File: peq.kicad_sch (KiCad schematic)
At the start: 0 parts

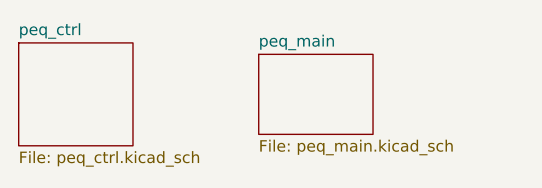
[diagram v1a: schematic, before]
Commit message: add protection components and fix layout
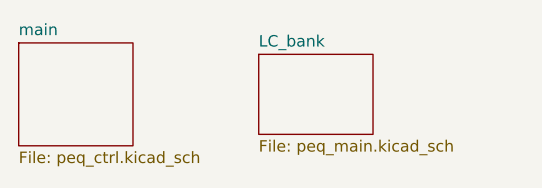
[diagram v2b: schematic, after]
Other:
- sheet peq_ctrl renamed main
- sheet peq_main renamed LC_bank
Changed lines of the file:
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@@
     (stroke (width 0.1524) (type solid) (color 0 0 0 0))
     (fill (color 0 0 0 0.0000))
-    (property "Sheet name" "peq_main" (id 0) (at 52.07 178.3584 0)
+    (property "Sheet name" "LC_bank" (id 0) (at 52.07 178.3584 0)
       (effects (font (size 1.27 1.27)) (justify left bottom))
     )
@@
     (stroke (width 0.1524) (type solid) (color 0 0 0 0))
     (fill (color 0 0 0 0.0000))
-    (property "Sheet name" "peq_ctrl" (id 0) (at 25.4 177.0884 0)
+    (property "Sheet name" "main" (id 0) (at 25.4 177.0884 0)
       (effects (font (size 1.27 1.27)) (justify left bottom))
     )
@@
       (reference "#FLG02") (unit 1) (value "PWR_FLAG") (footprint "")
     )
-    (path "/38f7f3f1-89e1-4fd2-a7f5-06bedaf10569/d5f17e22-8b80-4887-9e54-e1e00c7d3ac3"
+    (path "/bb76919e-6bfc-4ffb-bc2f-e672a0fcf05d/2d62a2ff-d101-4f92-af62-e6162c70abe7"
       (reference "#PWR01") (unit 1) (value "+VDC") (footprint "")
+    )
+    (path "/bb76919e-6bfc-4ffb-bc2f-e672a0fcf05d/9d7d23d0-20c5-40b7-81a1-a09f216d6c5f"
+      (reference "#PWR02") (unit 1) (value "GND") (footprint "")
+    )
+    (path "/bb76919e-6bfc-4ffb-bc2f-e672a0fcf05d/bde16bca-a34a-4bfd-a7c0-17ec97862e27"
+      (reference "#PWR03") (unit 1) (value "GND") (footprint "")
+    )
+    (path "/bb76919e-6bfc-4ffb-bc2f-e672a0fcf05d/dec3e4fc-6e35-4c2d-84a1-9853e1bdd326"
+      (reference "#PWR04") (unit 1) (value "GND") (footprint "")
+    )
+    (path "/bb76919e-6bfc-4ffb-bc2f-e672a0fcf05d/b2db637f-9949-414c-a3e0-a61ee3353909"
+      (reference "#PWR05") (unit 1) (value "GND") (footprint "")
     )
     (path "/bb76919e-6bfc-4ffb-bc2f-e672a0fcf05d/1409c838-f9a4-46df-90e0-6a7eb40eaef3"
@@
       (reference "#PWR024") (unit 1) (value "GND") (footprint "")
     )
-    (path "/38f7f3f1-89e1-4fd2-a7f5-06bedaf10569/be75252c-f03e-431d-b2b2-7e25a713ff1f"
-      (reference "#PWR0102") (unit 1) (value "GND") (footprint "")
-    )
     (path "/38f7f3f1-89e1-4fd2-a7f5-06bedaf10569/f585edc7-fb81-4473-a462-9d948cfe0732"
       (reference "C1") (unit 1) (value "56n") (footprint "Capacitor_THT:C_Rect_L7.2mm_W4.5mm_P5.00mm_FKS2_FKP2_MKS2_MKP2")
@@
       (reference "C36") (unit 1) (value "220n") (footprint "Capacitor_THT:C_Rect_L7.2mm_W3.5mm_P5.00mm_FKS2_FKP2_MKS2_MKP2")
     )
-    (path "/38f7f3f1-89e1-4fd2-a7f5-06bedaf10569/b776ed53-5630-4d5e-9d01-9e583c6b0db2"
+    (path "/bb76919e-6bfc-4ffb-bc2f-e672a0fcf05d/f43ff078-16a1-47b5-8360-0e2aa6e37ab6"
+      (reference "C37") (unit 1) (value "NC") (footprint "Capacitor_SMD:C_0805_2012Metric_Pad1.18x1.45mm_HandSolder")
+    )
+    (path "/bb76919e-6bfc-4ffb-bc2f-e672a0fcf05d/81a3d07a-4314-4383-bda9-b9ff99a33cd4"
+      (reference "C38") (unit 1) (value "0.1u") (footprint "Capacitor_SMD:C_0805_2012Metric_Pad1.18x1.45mm_HandSolder")
+    )
+    (path "/bb76919e-6bfc-4ffb-bc2f-e672a0fcf05d/d8c86677-4d44-400f-b2fd-6f8726205fcd"
+      (reference "C39") (unit 1) (value "0.1u") (footprint "Capacitor_SMD:C_0805_2012Metric_Pad1.18x1.45mm_HandSolder")
+    )
+    (path "/bb76919e-6bfc-4ffb-bc2f-e672a0fcf05d/8a2d3497-5886-4b2e-9885-2de1a2810bc2"
       (reference "D1") (unit 1) (value "LED") (footprint "LED_THT:LED_D3.0mm")
     )
     (path "/bb76919e-6bfc-4ffb-bc2f-e672a0fcf05d/201d10c3-7a33-4c01-8e86-1dfa9b6c4123"
-      (reference "D2") (unit 1) (value "D") (footprint "Diode_THT:D_DO-34_SOD68_P7.62mm_Horizontal")
+      (reference "D2") (unit 1) (value "D") (footprint "Diode_THT:D_DO-35_SOD27_P7.62mm_Horizontal")
+    )
+    (path "/bb76919e-6bfc-4ffb-bc2f-e672a0fcf05d/71f7701d-3e36-4518-8f6a-c08ff2205ea7"
+      (reference "D3") (unit 1) (value "D_Zener") (footprint "Diode_THT:D_DO-35_SOD27_P2.54mm_Vertical_AnodeUp")
+    )
+    (path "/bb76919e-6bfc-4ffb-bc2f-e672a0fcf05d/95980576-80aa-48c2-bd77-0fb522b1f4d3"
+      (reference "F1") (unit 1) (value "Polyfuse") (footprint "Resistor_THT:R_Axial_DIN0204_L3.6mm_D1.6mm_P5.08mm_Horizontal")
     )
     (path "/bb76919e-6bfc-4ffb-bc2f-e672a0fcf05d/2c1028e4-ebca-4ad3-bb8d-ff4be69d545c"
@@
       (reference "Q1") (unit 1) (value "2N3904") (footprint "Package_TO_SOT_THT:TO-92")
     )
-    (path "/38f7f3f1-89e1-4fd2-a7f5-06bedaf10569/b934a48c-4b4a-48f4-96f3-2de687c27954"
+    (path "/bb76919e-6bfc-4ffb-bc2f-e672a0fcf05d/3fb5c3b9-85cf-46ff-be12-fe6d1a53576d"
       (reference "R1") (unit 1) (value "47k") (footprint "ak_misc:R_Axial_DIN0207_L6.3mm_D2.5mm_P7.62mm_with_SMD")
     )
@@
       (reference "R8") (unit 1) (value "1Meg") (footprint "ak_misc:R_Axial_DIN0207_L6.3mm_D2.5mm_P7.62mm_with_SMD")
     )
+    (path "/bb76919e-6bfc-4ffb-bc2f-e672a0fcf05d/7ec7bfbb-e653-465e-8fa7-f004ee2793f3"
+      (reference "R9") (unit 1) (value "470k") (footprint "Resistor_SMD:R_0805_2012Metric_Pad1.20x1.40mm_HandSolder")
+    )
+    (path "/bb76919e-6bfc-4ffb-bc2f-e672a0fcf05d/b75f2a90-0628-49f1-87ca-36bfcc01cf71"
+      (reference "R10") (unit 1) (value "470k") (footprint "Resistor_SMD:R_0805_2012Metric_Pad1.20x1.40mm_HandSolder")
+    )
     (path "/bb76919e-6bfc-4ffb-bc2f-e672a0fcf05d/b58d268c-ae1d-4384-b061-cd10e7570604"
       (reference "R24") (unit 1) (value "47k") (footprint "ak_misc:R_Axial_DIN0207_L6.3mm_D2.5mm_P7.62mm_with_SMD")
@@
       (reference "RV6") (unit 1) (value "VOL:A1M") (footprint "ak_misc:POT-16mm")
     )
-    (path "/38f7f3f1-89e1-4fd2-a7f5-06bedaf10569/d3a840fa-d51f-45cb-9850-5fbb21eb4da9"
+    (path "/bb76919e-6bfc-4ffb-bc2f-e672a0fcf05d/ed97cd06-b141-42d6-8c73-7f46f4fff575"
       (reference "SW1") (unit 1) (value "3PDT_FootSwitch") (footprint "ak_misc:3PDT_FootSwitch_ovalpad")
     )
-    (path "/38f7f3f1-89e1-4fd2-a7f5-06bedaf10569/80a161fc-1b87-496a-9a39-0314de3beef8"
+    (path "/bb76919e-6bfc-4ffb-bc2f-e672a0fcf05d/51951a7b-6b9e-4685-b609-a5a2a5787d25"
       (reference "SW1") (unit 2) (value "3PDT_FootSwitch") (footprint "ak_misc:3PDT_FootSwitch_ovalpad")
     )
-    (path "/38f7f3f1-89e1-4fd2-a7f5-06bedaf10569/6a61121c-8930-4a5b-8bab-e0516d27744e"
+    (path "/bb76919e-6bfc-4ffb-bc2f-e672a0fcf05d/19797c1a-621b-4a94-83d9-d4dc6d9b5a4a"
       (reference "SW1") (unit 3) (value "3PDT_FootSwitch") (footprint "ak_misc:3PDT_FootSwitch_ovalpad")
     )

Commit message: update comments and credits
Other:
- company: (none) -> MST/mesotokyo
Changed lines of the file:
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@@
   (title_block
     (title "PEQ")
+    (date "2024-11-02")
+    (rev "v1.1")
+    (company "MST/mesotokyo")
+    (comment 1 "https://meso.tokyo/")
   )
   (sheet (at 52.07 179.07) (size 12.7 8.89) (fields_autoplaced)
